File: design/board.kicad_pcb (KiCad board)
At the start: 2 copper layers, 39.4 x 29.2 mm, 14 parts, among them J1 Barrel_Jack_Switch, J2 Conn_01x01_Male, J3 Conn_01x01_Male, J4 Conn_01x01_Male, J5 Conn_01x01_Male, SW1 main

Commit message: New pcb design.
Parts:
- removed J2, J3, J4, J5: Conn_01x01_Male, Connector_PinHeader_1.00mm:PinHeader_1x01_P1.00mm_Vertical
- added J6: Conn_01x04_Female, Connector_PinSocket_2.54mm:PinSocket_2x02_P2.54mm_Vertical, B.Cu at (182.0, 90.2)
- R1, R2, R3, R4: moved to B.Cu
- moved R3 50.5 mm to (182.9, 93.0), turned to 180 degrees
- moved D3 46.6 mm to (179.1, 97.8), turned to 90 degrees
- moved J1 43.7 mm to (165.9, 85.2), turned to 0 degrees
- moved R1 43.0 mm to (170.3, 92.2), turned to 0 degrees
- moved D2 39.2 mm to (173.2, 95.2), turned to 270 degrees
- moved C1 39.1 mm to (164.0, 78.0)
- moved R4 35.7 mm to (180.7, 85.1)
- moved D1 31.7 mm to (174.2, 88.8)
- moved R2 27.1 mm to (169.9, 75.9)
- moved SW1 21.6 mm to (173.7, 68.5)
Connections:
- net /+5V renamed /VCC_OUT
- net Net-(D1-Pad1) renamed /MID_PWR
- net Net-(D2-Pad2) renamed /MID_OFF
- net Net-(D3-Pad1) renamed /MID_ON
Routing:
- net GND: track 110.5 -> 2.63 mm, vias 2 -> 0
- net /VCC_OUT: track 98.4 -> 37.8 mm, vias 1 -> 0
- net VCC: track 62.4 -> 2.20 mm, vias 1 -> 0
- net /MID_OFF: track 6.88 -> 24.5 mm
- net /MID_PWR: track 7.39 -> 4.51 mm
- added copper zone on B.Cu, net GND
- added copper zone on F.Cu, net VCC
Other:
- board size 39.4 x 29.2 mm -> 24.9 x 31.6 mm

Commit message: Silk layer.
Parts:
- D1, D2, D3: moved to B.Cu
- moved R3 1.20 mm to (183.4, 94.1), turned to 90 degrees
- moved D2 1.14 mm to (173.2, 94.1)
- moved D3 1.14 mm to (179.1, 96.6)
- moved R1 0.64 mm to (170.4, 91.6)
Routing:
- net /MID_ON: track 7.56 -> 4.77 mm
- net /MID_OFF: track 24.5 -> 23.7 mm
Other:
- board text added: "OFF"
- board text added: "ON"
- board text added: "ON / OFF"
- board text added: "PWR"

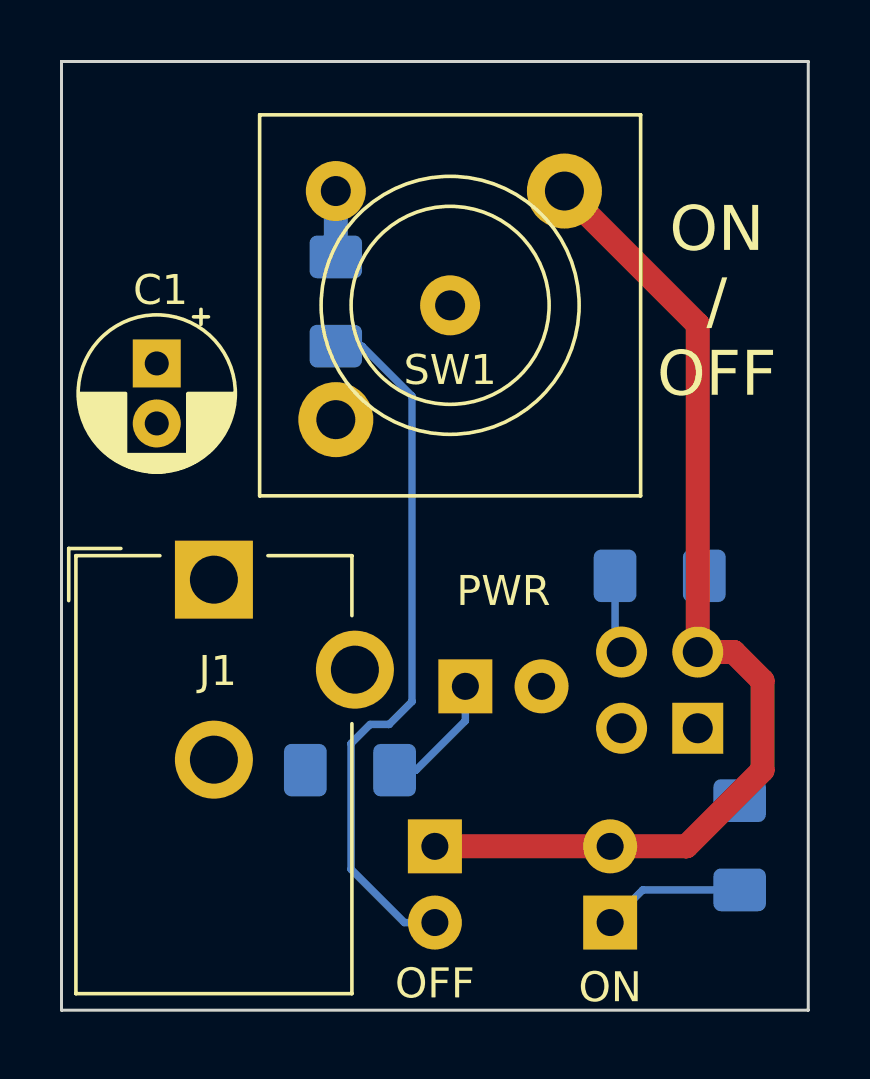
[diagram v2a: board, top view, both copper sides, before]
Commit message: Correct DC connector + slide switch + image update.
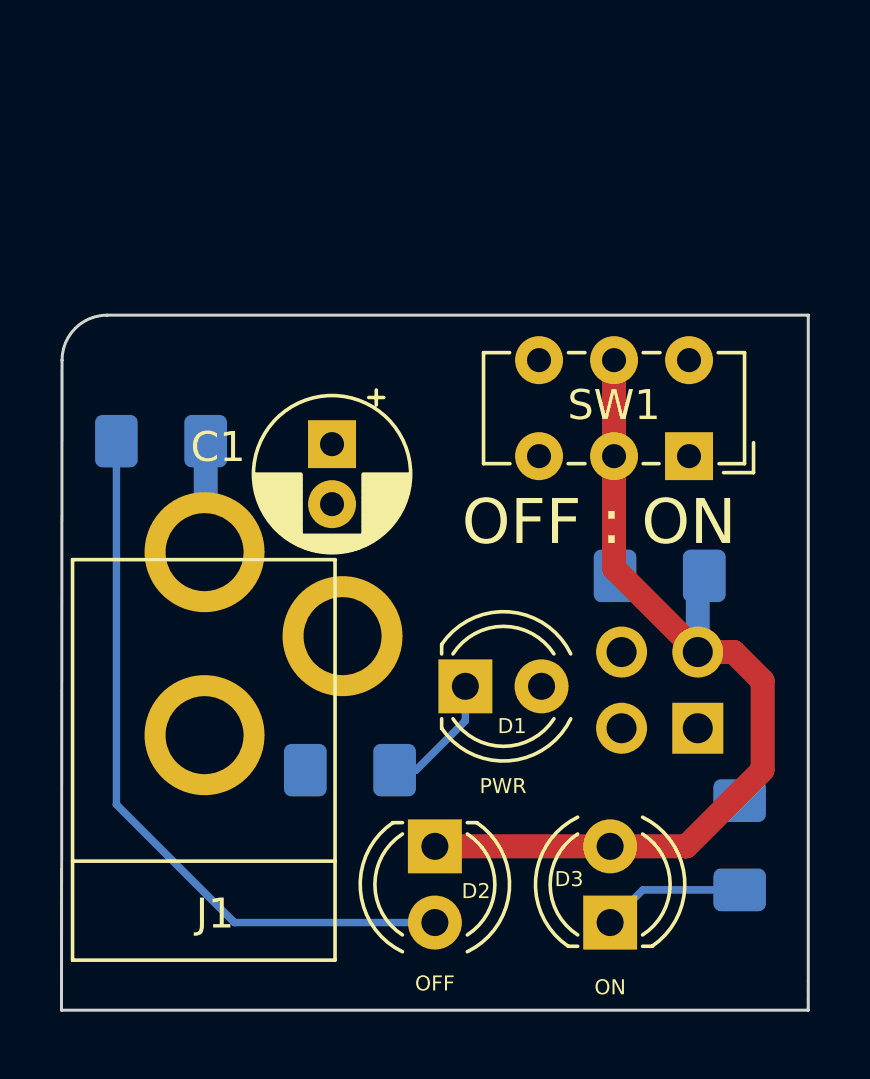
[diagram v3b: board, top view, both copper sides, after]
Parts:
- D1, D2, D3: moved to F.Cu
- J1: footprint Connector_BarrelJack:BarrelJack_CUI_PJ-102AH_Horizontal -> my_power:DC_barrel_2.1x5.5d
- SW1: footprint my_buttons:pushbutton_switch -> Button_Switch_THT:SW_E-Switch_EG1271_DPDT
- moved SW1 14.9 mm to (181.7, 81.1), turned to 180 degrees
- moved J1 10.8 mm to (166.7, 96.0)
- moved R2 7.46 mm to (164.1, 80.6), turned to 180 degrees
- moved C1 6.43 mm to (169.8, 80.7)
- renumbered J6 to J2
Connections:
- J1 pad 1: GND -> VCC
- J1 pad 3: VCC -> GND
- SW1 pad 3: (no net) -> GND
- SW1 pad 4: (no net) -> VCC
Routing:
- net /VCC_OUT: track 37.3 -> 31.0 mm
- net GND: track 2.63 -> 0.31 mm
- net VCC: track 2.20 -> 3.72 mm
- net /MID_OFF: track 23.7 -> 24.4 mm
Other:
- board size 24.9 x 31.6 mm -> 24.9 x 23.2 mm
- board text added: "OFF : ON"
- board text removed: "ON / OFF"
